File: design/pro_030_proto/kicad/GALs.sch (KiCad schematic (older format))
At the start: 19 parts, among them IC10 ATF22V10C, IC14 ATF22V10C, IC2 ATF22V10C, IC3 ATF22V10C, IC4 ATF22V10C, IC5 ATF22V10C, IC6 ATF22V10C, IC7 ATF22V10C

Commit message: Rerate DTn resistors
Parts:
- R24, R25, R26: value 4K7 -> 1K2
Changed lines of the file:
@@
 P 1400 6900
 F 0 "R24" H 1470 6946 50  0000 L CNN
-F 1 "4K7" H 1470 6855 50  0000 L CNN
+F 1 "1K2" H 1470 6855 50  0000 L CNN
 F 2 "rosco_m68k:R-0207_10" V 1330 6900 50  0001 C CNN
 F 3 "~" H 1400 6900 50  0001 C CNN
@@
 P 1700 6900
 F 0 "R25" H 1770 6946 50  0000 L CNN
-F 1 "4K7" H 1770 6855 50  0000 L CNN
+F 1 "1K2" H 1770 6855 50  0000 L CNN
 F 2 "rosco_m68k:R-0207_10" V 1630 6900 50  0001 C CNN
 F 3 "~" H 1700 6900 50  0001 C CNN
@@
 P 2000 6900
 F 0 "R26" H 2070 6946 50  0000 L CNN
-F 1 "4K7" H 2070 6855 50  0000 L CNN
+F 1 "1K2" H 2070 6855 50  0000 L CNN
 F 2 "rosco_m68k:R-0207_10" V 1930 6900 50  0001 C CNN
 F 3 "~" H 2000 6900 50  0001 C CNN

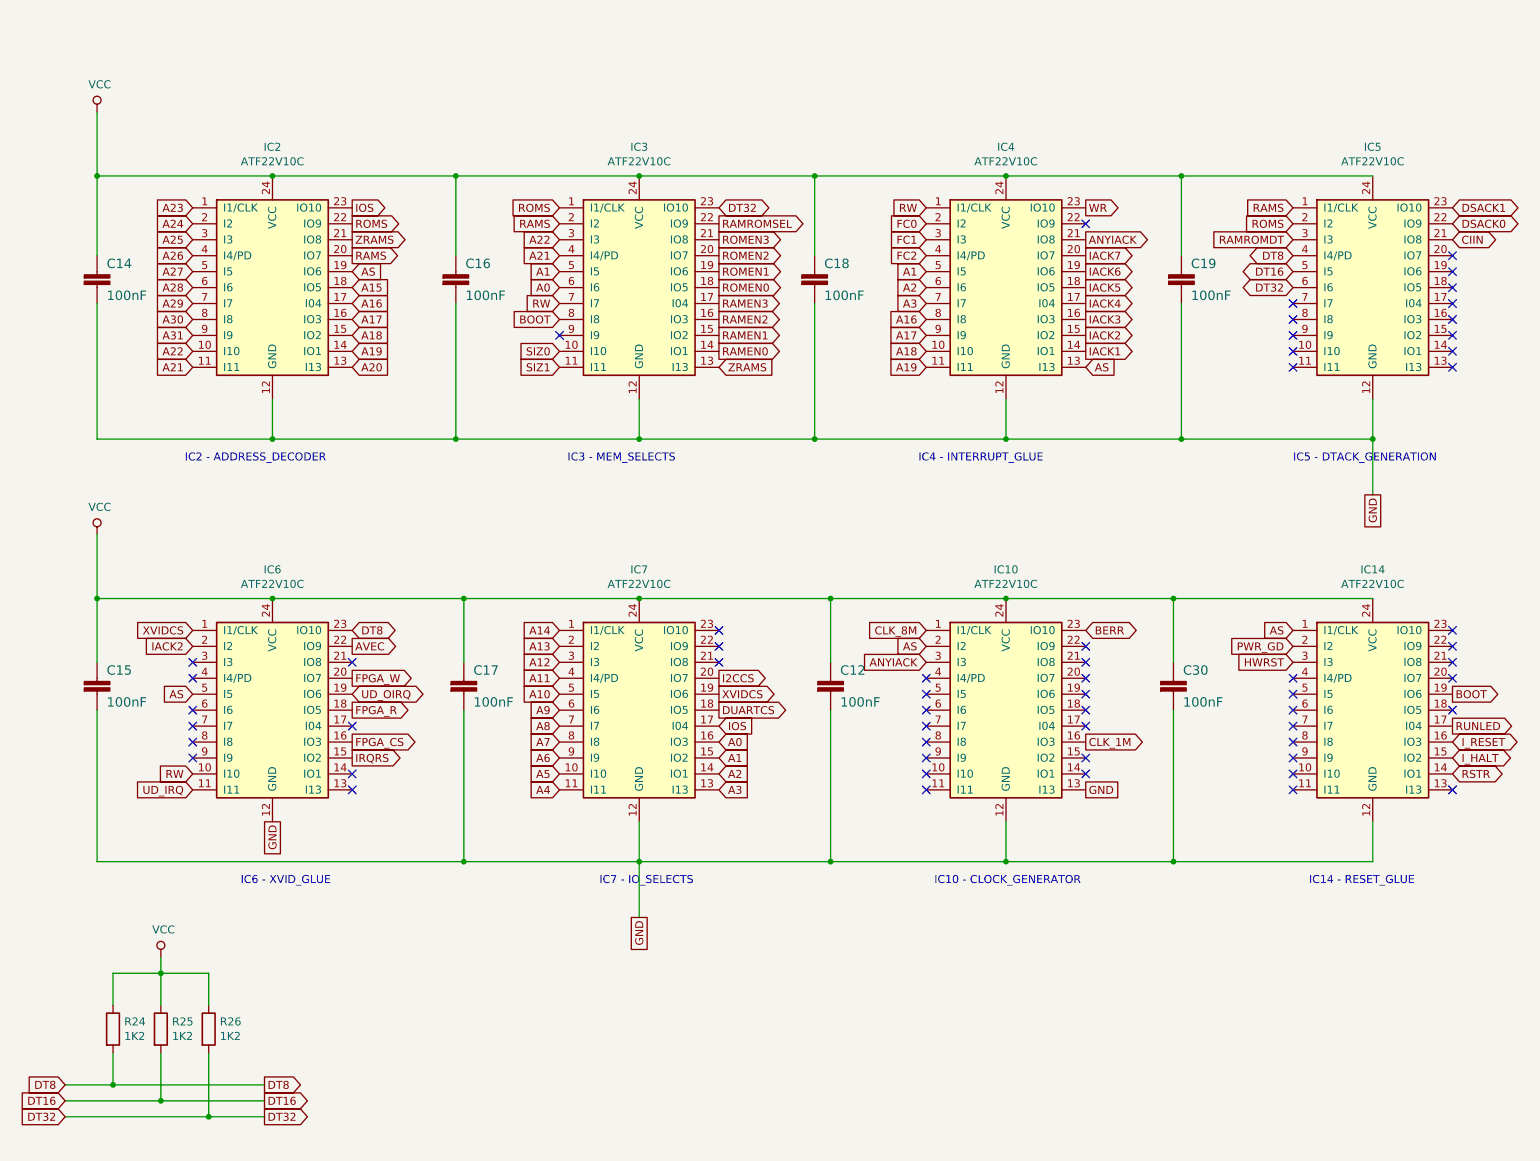
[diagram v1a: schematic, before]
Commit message: Add new Xosera DTACK stretch GAL
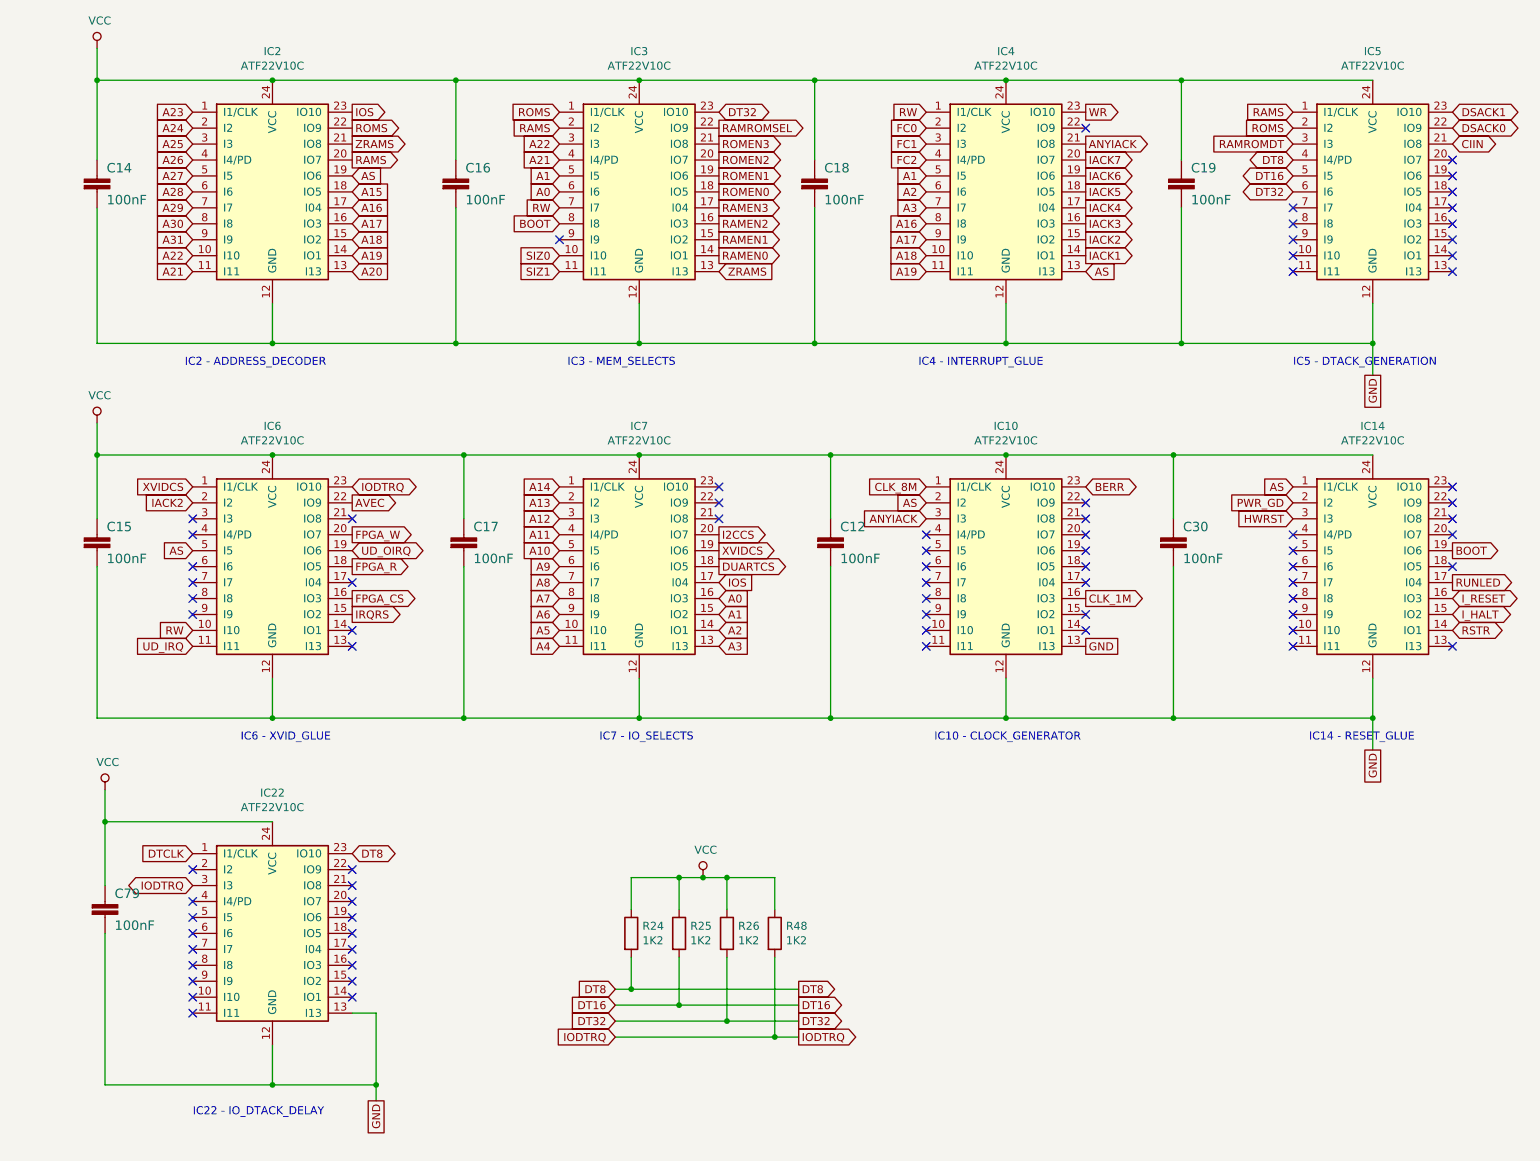
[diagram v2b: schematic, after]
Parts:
- added C79: 100nF, Capacitor_THT:C_Rect_L4.0mm_W2.5mm_P2.50mm, symbol rosco_m68k-eagle-import:C2,5-3
- added IC22: ATF22V10C, Package_DIP:DIP-24_W7.62mm_Socket_LongPads, symbol rosco_m68k:GAL22V10
- added R48: 1K2, rosco_m68k:R-0207_10, symbol Device:R
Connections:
- net DT8: now also IC22.23 (IO10); no longer IC6.23 (IO10)
- net GND: now also C79.2, IC22.12 (GND), IC22.13 (I13)
- net VCC: now also C79.1, IC22.24 (VCC), R48.1
- new net DTCLK: IC22.1 (I1/CLK)
- new net IODTRQ: IC22.3 (I3), IC6.23 (IO10), R48.2
- no-connect marks 58 -> 76
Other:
- note added: "IC22 - IO_DTACK_DELAY"
- moved on the sheet: C12, C14, C15, C16, C17, C18, C19, C30, IC10, IC14, IC2, IC3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
